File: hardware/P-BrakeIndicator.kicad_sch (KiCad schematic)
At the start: 13 parts, among them J1 -PRW+, J2 RX TX, J3 +SPK-, J4 Ir.In, Q1 2N7000, U1 ATtiny202

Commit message: pcb: widen power traces and relocate hardware project assets
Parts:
- R4: value 10 Omh -> 10.Om
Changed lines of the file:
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@@
 			)
 		)
-		(property "Value" "10 Omh"
+		(property "Value" "10.Om"
 			(at 163.068 65.532 90)
 			(show_name no)

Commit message: pcb: update component values and increase track widths to 0.5mm
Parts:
- R3: value 0.1k -> 50Ω
- R4: value 10.Om -> 10Ω
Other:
- moved on the sheet: J1
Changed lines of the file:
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@@
+	)
+	(junction
+		(at 134.62 26.67)
+		(diameter 0)
+		(color 0 0 0 0)
+	)
+	(junction
+		(at 134.62 85.09)
+		(diameter 0)
+		(color 0 0 0 0)
 	)
 	(junction
@@
 	)
 	(junction
-		(at 134.62 26.67)
+		(at 177.8 68.58)
 		(diameter 0)
 		(color 0 0 0 0)
 	)
 	(junction
-		(at 134.62 85.09)
+		(at 167.64 82.55)
 		(diameter 0)
 		(color 0 0 0 0)
@@
 	)
 	(junction
-		(at 177.8 68.58)
-		(diameter 0)
-		(color 0 0 0 0)
-	)
-	(junction
-		(at 167.64 82.55)
-		(diameter 0)
-		(color 0 0 0 0)
-	)
-	(junction
 		(at 167.64 63.5)
 		(diameter 0)
@@
 	(wire
 		(pts
-			(xy 119.38 85.09) (xy 114.3 85.09)
-		)
-		(stroke
-			(width 0)
-			(type default)
-		)
-	)
-	(wire
-		(pts
 			(xy 167.64 82.55) (xy 134.62 82.55)
 		)
@@
 	(wire
 		(pts
-			(xy 99.06 57.15) (xy 119.38 57.15)
+			(xy 115.57 50.8) (xy 119.38 50.8)
 		)
 		(stroke
@@
 	(wire
 		(pts
-			(xy 119.38 57.15) (xy 119.38 85.09)
+			(xy 119.38 50.8) (xy 119.38 85.09)
+		)
+		(stroke
+			(width 0)
+			(type default)
+		)
+	)
+	(wire
+		(pts
+			(xy 119.38 48.26) (xy 115.57 48.26)
 		)
 		(stroke
@@
 	(wire
 		(pts
-			(xy 114.3 85.09) (xy 114.3 90.17)
+			(xy 119.38 85.09) (xy 119.38 90.17)
 		)
 		(stroke
@@
 	(wire
 		(pts
-			(xy 99.06 26.67) (xy 134.62 26.67)
+			(xy 119.38 26.67) (xy 134.62 26.67)
 		)
 		(stroke
@@
 	(wire
 		(pts
-			(xy 134.62 85.09) (xy 134.62 88.9)
-		)
-		(stroke
-			(width 0)
-			(type default)
-		)
-	)
-	(wire
-		(pts
-			(xy 99.06 54.61) (xy 99.06 26.67)
+			(xy 134.62 85.09) (xy 134.62 90.17)
+		)
+		(stroke
+			(width 0)
+			(type default)
+		)
+	)
+	(wire
+		(pts
+			(xy 119.38 48.26) (xy 119.38 26.67)
 		)
 		(stroke
@@
 			)
 		)
-		(property "Value" "10.Om"
+		(property "Value" "10Ω"
 			(at 163.068 65.532 90)
 			(show_name no)
@@
 	(symbol
 		(lib_id "power:GND")
-		(at 134.62 88.9 0)
+		(at 134.62 90.17 0)
 		(unit 1)
 		(body_style 1)
@@
 		(fields_autoplaced yes)
 		(property "Reference" "#PWR01"
+			(at 134.62 96.52 0)
+			(hide yes)
+			(show_name no)
+			(do_not_autoplace no)
+			(effects
+				(font
+					(size 1.27 1.27)
+				)
+			)
+		)
+		(property "Value" "GND"
 			(at 134.62 95.25 0)
-			(hide yes)
-			(show_name no)
-			(do_not_autoplace no)
-			(effects
-				(font
-					(size 1.27 1.27)
-				)
-			)
-		)
-		(property "Value" "GND"
-			(at 134.62 93.98 0)
 			(show_name no)
 			(do_not_autoplace no)
@@
 		)
 		(property "Footprint" ""
-			(at 134.62 88.9 0)
+			(at 134.62 90.17 0)
 			(hide yes)
 			(show_name no)
@@
 		)
 		(property "Datasheet" ""
-			(at 134.62 88.9 0)
+			(at 134.62 90.17 0)
 			(hide yes)
 			(show_name no)
@@
 		)
 		(property "Description" "Power symbol creates a global label with name \"GND\" , ground"
-			(at 134.62 88.9 0)
+			(at 134.62 90.17 0)
 			(hide yes)
 			(show_name no)
@@
 	(symbol
 		(lib_id "Connector:Conn_01x02_Pin")
-		(at 93.98 54.61 0)
+		(at 110.49 48.26 0)
 		(unit 1)
 		(body_style 1)
@@
 		(dnp no)
 		(property "Reference" "J1"
-			(at 90.424 55.88 90)
+			(at 106.934 49.53 90)
 			(show_name no)
 			(do_not_autoplace no)
@@
 		)
 		(property "Value" "-PRW+"
-			(at 92.71 55.372 90)
+			(at 109.22 49.022 90)
 			(show_name no)
 			(do_not_autoplace no)
@@
 		)
 		(property "Footprint" "Connector_PinHeader_2.54mm:PinHeader_1x02_P2.54mm_Vertical"
-			(at 93.98 54.61 0)
+			(at 110.49 48.26 0)
 			(hide yes)
 			(show_name no)
@@
 		)
 		(property "Datasheet" ""
-			(at 93.98 54.61 0)
+			(at 110.49 48.26 0)
 			(hide yes)
 			(show_name no)
@@
 		)
 		(property "Description" "Generic connector, single row, 01x02, script generated"
-			(at 93.98 54.61 0)
+			(at 110.49 48.26 0)
 			(hide yes)
 			(show_name no)
@@
 			)
 		)
-		(property "Value" "0.1k"
+		(property "Value" "50Ω"
 			(at 166.624 33.274 90)
 			(show_name no)
@@
 	(symbol
 		(lib_id "power:PWR_FLAG")
-		(at 114.3 90.17 180)
+		(at 119.38 90.17 180)
 		(unit 1)
 		(body_style 1)
@@
 		(in_pos_files yes)
 		(dnp no)
-		(fields_autoplaced yes)
 		(property "Reference" "#FLG02"
-			(at 114.3 92.075 0)
+			(at 119.38 92.075 0)
 			(hide yes)
 			(show_name no)
@@
 		)
 		(property "Value" "PWR_FLAG"
-			(at 116.84 91.4399 0)
+			(at 115.824 95.25 0)
 			(show_name no)
 			(do_not_autoplace no)
@@
 		)
 		(property "Footprint" ""
-			(at 114.3 90.17 0)
+			(at 119.38 90.17 0)
 			(hide yes)
 			(show_name no)
@@
 		)
 		(property "Datasheet" ""
-			(at 114.3 90.17 0)
+			(at 119.38 90.17 0)
 			(hide yes)
 			(show_name no)
@@
 		)
 		(property "Description" "Special symbol for telling ERC where power comes from"
-			(at 114.3 90.17 0)
-			(hide yes)
-			(show_name no)
+			(at 119.38 90.17 0)
+			(hide yes)
+			(show_name no)

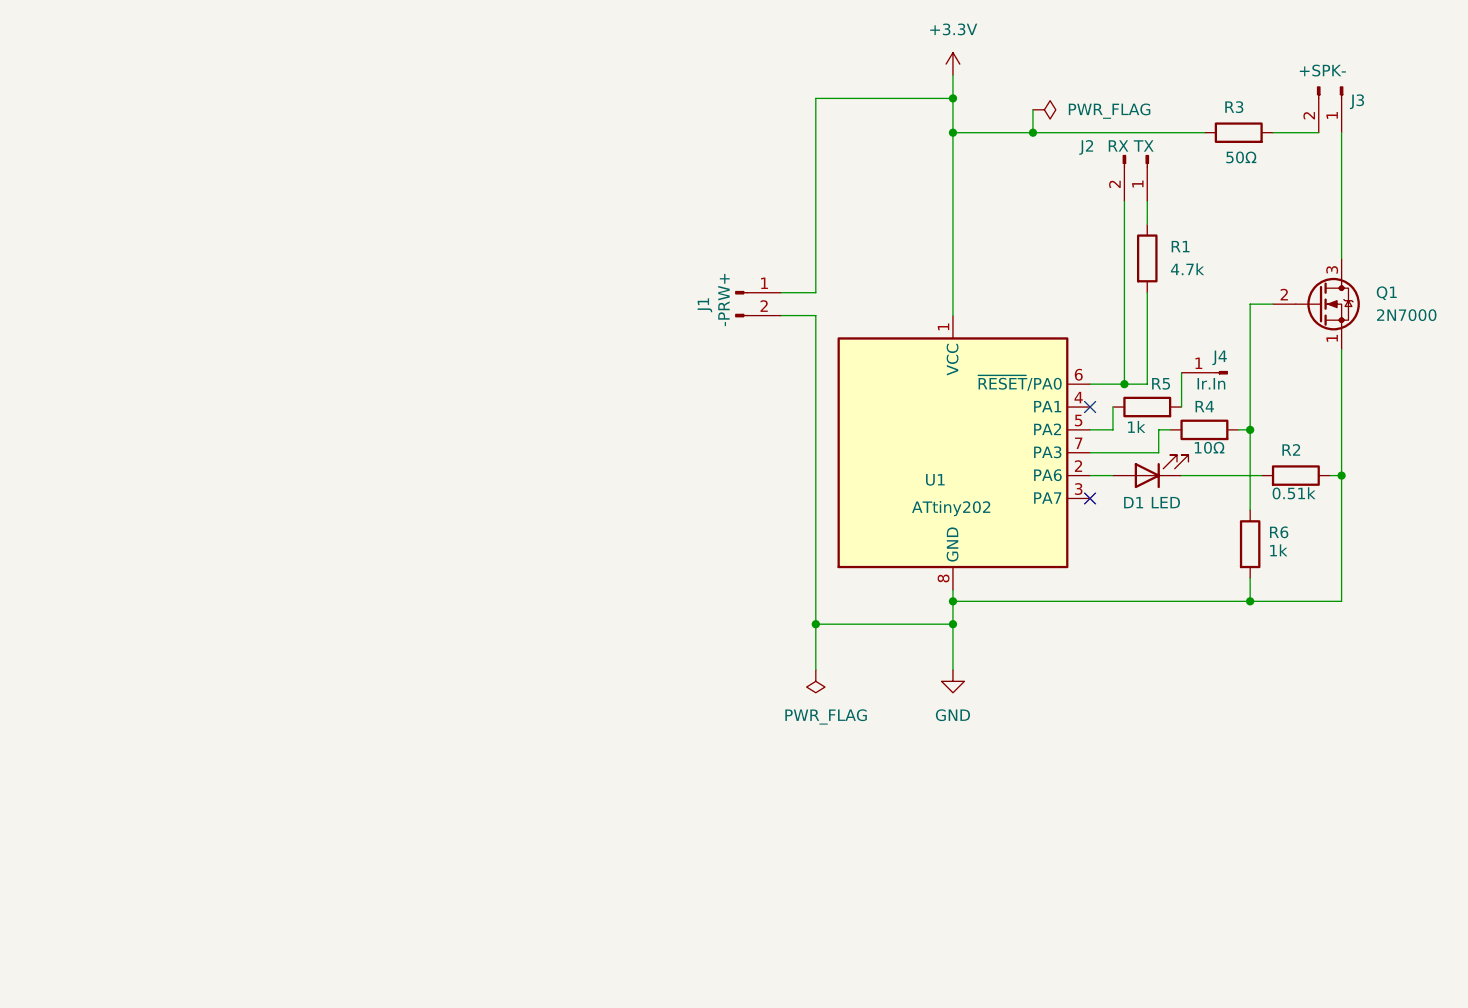
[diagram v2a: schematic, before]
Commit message: refactor: redesign board for comparator and carrier frequency
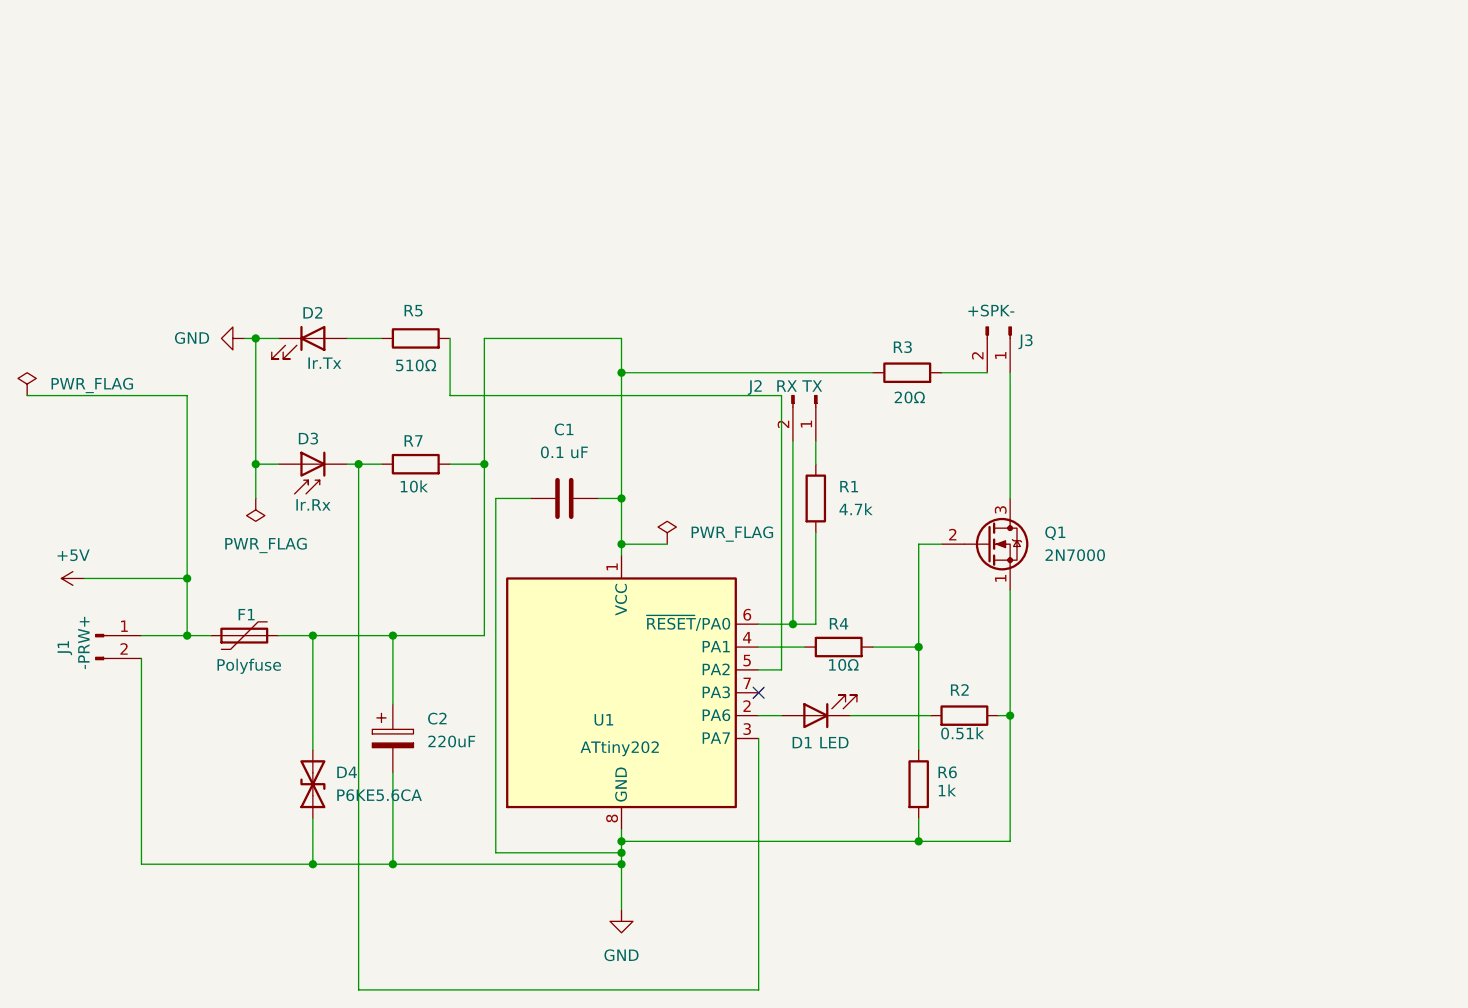
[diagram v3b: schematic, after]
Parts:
- removed J4: Ir.In, Connector_PinHeader_2.54mm:PinHeader_1x01_P2.54mm_Vertical, symbol Connector:Conn_01x01_Pin
- added C1: 0.1 uF, Capacitor_THT:C_Disc_D5.0mm_W2.5mm_P5.00mm, symbol Device:C
- added C2: 220uF, Capacitor_THT:CP_Radial_D5.0mm_P2.00mm, symbol Device:C_Polarized
- added D2: Ir.Tx, LED_THT:LED_D3.0mm, symbol Device:LED
- added D3: Ir.Rx, LED_THT:LED_D3.0mm, symbol Device:D_Photo
- added D4: P6KE5.6CA, Diode_THT:D_T-1_P5.08mm_Horizontal, symbol Device:D_TVS
- added F1: Polyfuse, Capacitor_THT:C_Disc_D5.0mm_W2.5mm_P5.00mm, symbol Device:Polyfuse
- added R7: 10k, Resistor_THT:R_Axial_DIN0207_L6.3mm_D2.5mm_P7.62mm_Horizontal, symbol Device:R
- D1: footprint LED_THT:LED_D5.0mm -> LED_THT:LED_D3.0mm
- R3: value 50Ω -> 20Ω
- R5: value 1k -> 510Ω
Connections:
- net GND: now also C1.1, C2.2, D2.1 (K), D3.2 (A), D4.1 (A1)
- net at R4.1: now also U1.4 (PA1); no longer U1.7 (PA3)
- net at U1.3 (PA7): now also D3.1 (K), R7.1
- net at U1.5 (PA2): now also R5.2; no longer R5.1
- net +3.3V: no longer names the net of R3.1, U1.1 (VCC)
- net +3.3V: now also C1.2, C2.1, D4.2 (A2), F1.2, R7.2; no longer J1.1 (Pin_1)
- new net: D2.2 (A), R5.1
- new net +5V: F1.1, J1.1 (Pin_1)
- no-connect marks 2 -> 1
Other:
- moved on the sheet: D1, J1, J2, J3, Q1, R1, R2, R3, R4, R6, U1
